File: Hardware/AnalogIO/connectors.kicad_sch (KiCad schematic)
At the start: 4 parts, among them J1 Conn_02x23_Odd_Even, J2 Conn_02x23_Odd_Even, J5 ANALOG INPUTS, J6 ANALOG OUTPUTS

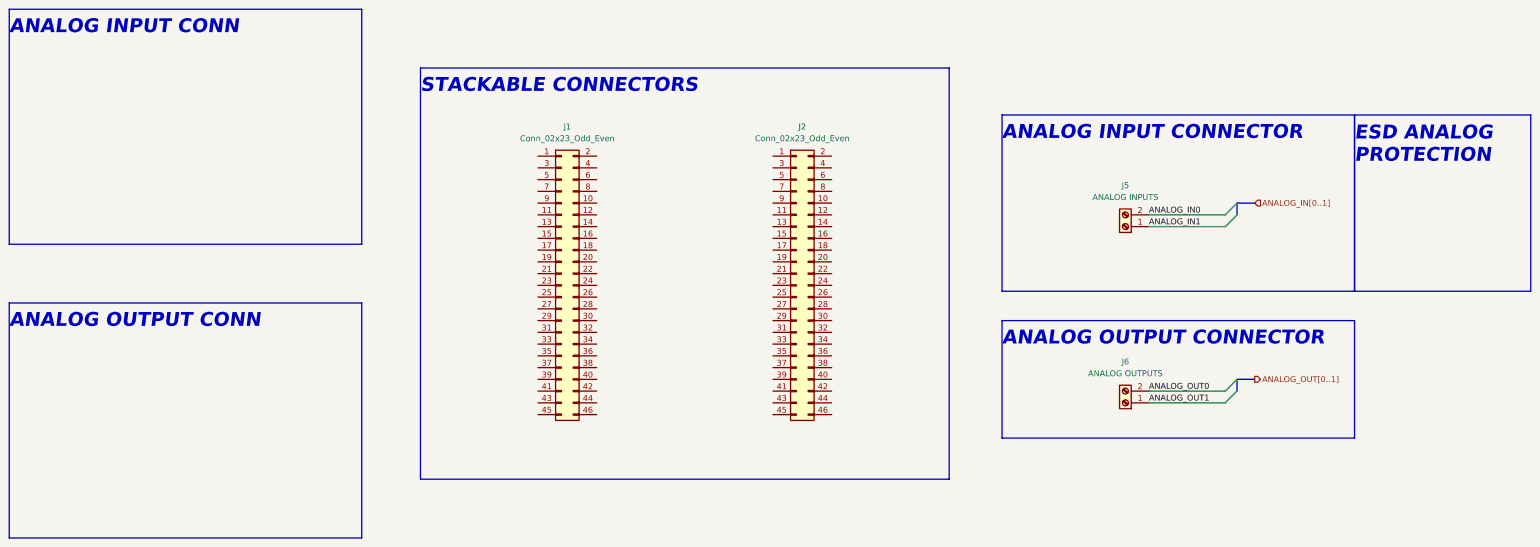
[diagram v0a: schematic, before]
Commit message: schematic update - all pcbs
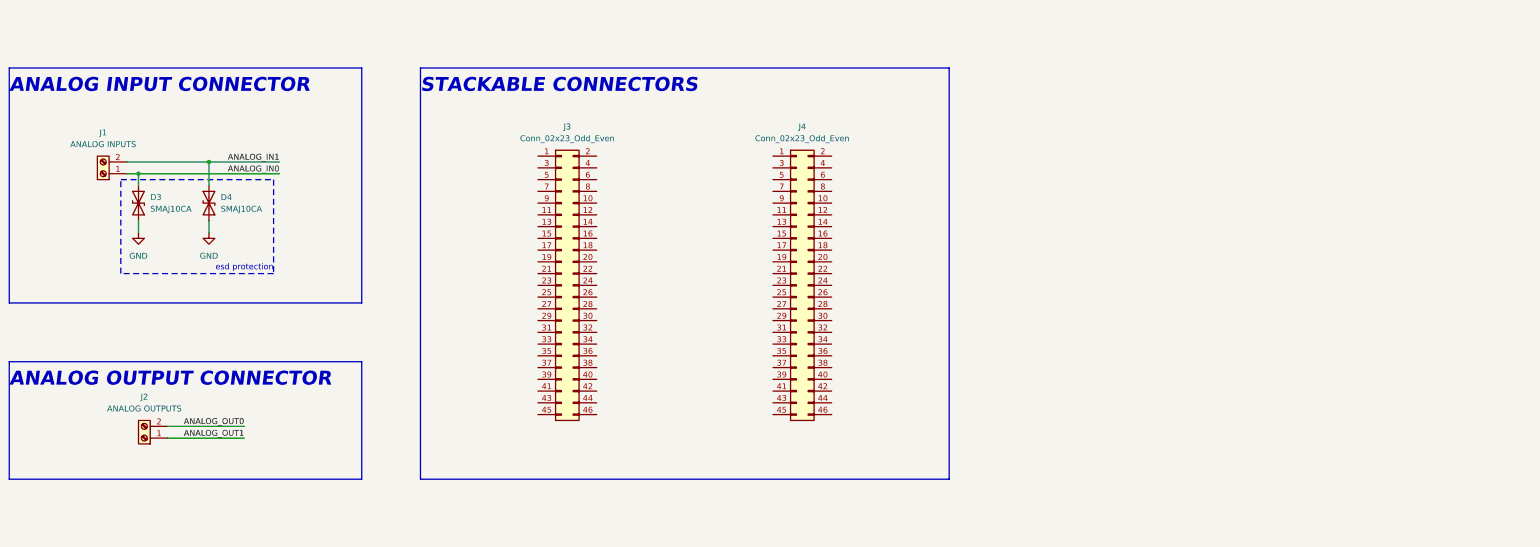
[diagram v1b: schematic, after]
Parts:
- added D3, D4: SMAJ10CA, Diode_SMD:D_SMA, symbol Diode:SMAJ10CA
- renumbered J5 to J1, J6 to J2, J1 to J3, J2 to J4
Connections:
- net ANALOG_IN0: now also J1.1 (Pin_1), D3.2 (A2); no longer J1.2 (Pin_2)
- net ANALOG_IN1: now also J1.2 (Pin_2), D4.1 (A1); no longer J1.1 (Pin_1)
- new net GND: D3.1 (A1), D4.2 (A2)
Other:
- note added: "esd protection"
- note removed: "ANALOG INPUT CONN"
- note removed: "ANALOG OUTPUT CONN"
- note removed: "ESD ANALOG PROTECTION"
- moved on the sheet: J1, J2
